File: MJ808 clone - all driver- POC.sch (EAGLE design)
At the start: 38 parts, among them IC1 ATTINY4313-MMH, IC2 PRQV8.00CR1510Y00L, IC6 MCP2515, IC7 MAX16820, IC8 MCP2561-2, IC9 TPS709-Q1, K1 CRTL, Q1 PMV213SN,215, X1 22-23-2021, X2 22-23-2021

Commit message: - updated values for LED1 and LED2, re-generated gerbers
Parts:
- LED1: value XMLBWT-00-0000-0000U20E2 -> LTST-C281KRKT
- LED2: value XMLBWT-00-0000-0000U20E2 -> LTST-C281KGKT
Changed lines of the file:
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@@
 <part name="IC9" library="TPS709-q1 5V LDO" deviceset="TPS709-Q1" device="" value="TPS709-Q1"/>
 <part name="R1" library="rcl" library_urn="urn:adsk.eagle:library:334" deviceset="R-EU_" device="R0402" package3d_urn="urn:adsk.eagle:package:23547/1" value="10k"/>
-<part name="LED1" library="led" library_urn="urn:adsk.eagle:library:259" deviceset="LED" device="CHIP-LED0805" package3d_urn="urn:adsk.eagle:package:15818/1" value="XMLBWT-00-0000-0000U20E2 "/>
-<part name="LED2" library="led" library_urn="urn:adsk.eagle:library:259" deviceset="LED" device="CHIP-LED0805" package3d_urn="urn:adsk.eagle:package:15818/1" value="XMLBWT-00-0000-0000U20E2 "/>
+<part name="LED1" library="led" library_urn="urn:adsk.eagle:library:259" deviceset="LED" device="CHIP-LED0805" package3d_urn="urn:adsk.eagle:package:15818/1" value="LTST-C281KRKT"/>
+<part name="LED2" library="led" library_urn="urn:adsk.eagle:library:259" deviceset="LED" device="CHIP-LED0805" package3d_urn="urn:adsk.eagle:package:15818/1" value="LTST-C281KGKT"/>
 <part name="R3" library="rcl" library_urn="urn:adsk.eagle:library:334" deviceset="R-EU_" device="R0402" package3d_urn="urn:adsk.eagle:package:23547/1" value="10k"/>
 <part name="R4" library="rcl" library_urn="urn:adsk.eagle:library:334" deviceset="R-EU_" device="R0402" package3d_urn="urn:adsk.eagle:package:23547/1" value="10k"/>

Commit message: - sized down ground plane of ICs to make soldering easier - corrected tname and bname positions
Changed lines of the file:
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@@
 <?xml version="1.0" encoding="utf-8"?>
 <!DOCTYPE eagle SYSTEM "eagle.dtd">
-<eagle version="8.5.0">
+<eagle version="8.6.1">
 <drawing>
 <settings>

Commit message: - added pulldown on 5V LDO enable pin
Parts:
- added R5: 10k, rcl:R-EU_R0402
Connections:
- net EN: now also R5.2
- net GND: now also R5.1
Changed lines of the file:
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@@
 <part name="C5" library="rcl" library_urn="urn:adsk.eagle:library:334" deviceset="C-EU" device="C0402" package3d_urn="urn:adsk.eagle:package:23626/1" value="0.1μF"/>
 <part name="C1" library="rcl" library_urn="urn:adsk.eagle:library:334" deviceset="C-EU" device="C0402" package3d_urn="urn:adsk.eagle:package:23626/1" value="0.1μF"/>
-<part name="R11" library="rcl" library_urn="urn:adsk.eagle:library:334" deviceset="R-EU_" device="R0402" package3d_urn="urn:adsk.eagle:package:23547/1" value="10k"/>
-<part name="R7" library="rcl" library_urn="urn:adsk.eagle:library:334" deviceset="R-EU_" device="R0402" package3d_urn="urn:adsk.eagle:package:23547/1" value="10k"/>
-<part name="R2" library="rcl" library_urn="urn:adsk.eagle:library:334" deviceset="R-EU_" device="R0402" package3d_urn="urn:adsk.eagle:package:23547/1" value="10k"/>
+<part name="R11" library="rcl" library_urn="urn:adsk.eagle:library:334" deviceset="R-EU_" device="R0402" package3d_urn="urn:adsk.eagle:package:23547/2" value="10k"/>
+<part name="R7" library="rcl" library_urn="urn:adsk.eagle:library:334" deviceset="R-EU_" device="R0402" package3d_urn="urn:adsk.eagle:package:23547/2" value="10k"/>
+<part name="R2" library="rcl" library_urn="urn:adsk.eagle:library:334" deviceset="R-EU_" device="R0402" package3d_urn="urn:adsk.eagle:package:23547/2" value="10k"/>
 <part name="LSP1" library="solpad" library_urn="urn:adsk.eagle:library:364" deviceset="LSP10" device="" package3d_urn="urn:adsk.eagle:package:26501/1"/>
 <part name="LSP2" library="solpad" library_urn="urn:adsk.eagle:library:364" deviceset="LSP10" device="" package3d_urn="urn:adsk.eagle:package:26501/1"/>
@@
 <part name="IC2" library="PRQV8.00CR1510Y00L - 8MHz resonator" deviceset="PRQV" device="" value=" PRQV8.00CR1510Y00L"/>
 <part name="PROG" library="SPI 1.27mm 10pin header" deviceset="SPI-1.27-10-PIN-HEADER" device=""/>
-<part name="R9" library="rcl" library_urn="urn:adsk.eagle:library:334" deviceset="R-EU_" device="R0402" package3d_urn="urn:adsk.eagle:package:23547/1" value="330"/>
-<part name="R8" library="rcl" library_urn="urn:adsk.eagle:library:334" deviceset="R-EU_" device="R0402" package3d_urn="urn:adsk.eagle:package:23547/1" value="330"/>
-<part name="R6" library="rcl" library_urn="urn:adsk.eagle:library:334" deviceset="R-EU_" device="R0402" package3d_urn="urn:adsk.eagle:package:23547/1" value="330"/>
-<part name="R12" library="rcl" library_urn="urn:adsk.eagle:library:334" deviceset="R-EU_" device="R0402" package3d_urn="urn:adsk.eagle:package:23547/1" value="10k"/>
+<part name="R9" library="rcl" library_urn="urn:adsk.eagle:library:334" deviceset="R-EU_" device="R0402" package3d_urn="urn:adsk.eagle:package:23547/2" value="330"/>
+<part name="R8" library="rcl" library_urn="urn:adsk.eagle:library:334" deviceset="R-EU_" device="R0402" package3d_urn="urn:adsk.eagle:package:23547/2" value="330"/>
+<part name="R6" library="rcl" library_urn="urn:adsk.eagle:library:334" deviceset="R-EU_" device="R0402" package3d_urn="urn:adsk.eagle:package:23547/2" value="330"/>
+<part name="R12" library="rcl" library_urn="urn:adsk.eagle:library:334" deviceset="R-EU_" device="R0402" package3d_urn="urn:adsk.eagle:package:23547/2" value="10k"/>
 <part name="MOSI" library="signal testpoint" deviceset="TP" device="" value="cs"/>
 <part name="MISO" library="signal testpoint" deviceset="TP" device="" value="cs"/>
 <part name="IC9" library="TPS709-q1 5V LDO" deviceset="TPS709-Q1" device="" value="TPS709-Q1"/>
-<part name="R1" library="rcl" library_urn="urn:adsk.eagle:library:334" deviceset="R-EU_" device="R0402" package3d_urn="urn:adsk.eagle:package:23547/1" value="10k"/>
-<part name="LED1" library="led" library_urn="urn:adsk.eagle:library:259" deviceset="LED" device="CHIP-LED0805" package3d_urn="urn:adsk.eagle:package:15818/1" value="LTST-C281KRKT"/>
-<part name="LED2" library="led" library_urn="urn:adsk.eagle:library:259" deviceset="LED" device="CHIP-LED0805" package3d_urn="urn:adsk.eagle:package:15818/1" value="LTST-C281KGKT"/>
-<part name="R3" library="rcl" library_urn="urn:adsk.eagle:library:334" deviceset="R-EU_" device="R0402" package3d_urn="urn:adsk.eagle:package:23547/1" value="10k"/>
-<part name="R4" library="rcl" library_urn="urn:adsk.eagle:library:334" deviceset="R-EU_" device="R0402" package3d_urn="urn:adsk.eagle:package:23547/1" value="10k"/>
+<part name="R1" library="rcl" library_urn="urn:adsk.eagle:library:334" deviceset="R-EU_" device="R0402" package3d_urn="urn:adsk.eagle:package:23547/2" value="10k"/>
+<part name="LED1" library="led" library_urn="urn:adsk.eagle:library:259" deviceset="LED" device="CHIP-LED0805" package3d_urn="urn:adsk.eagle:package:15818/2" value="LTST-C281KRKT"/>
+<part name="LED2" library="led" library_urn="urn:adsk.eagle:library:259" deviceset="LED" device="CHIP-LED0805" package3d_urn="urn:adsk.eagle:package:15818/2" value="LTST-C281KGKT"/>
+<part name="R3" library="rcl" library_urn="urn:adsk.eagle:library:334" deviceset="R-EU_" device="R0402" package3d_urn="urn:adsk.eagle:package:23547/2" value="10k"/>
+<part name="R4" library="rcl" library_urn="urn:adsk.eagle:library:334" deviceset="R-EU_" device="R0402" package3d_urn="urn:adsk.eagle:package:23547/2" value="10k"/>
 <part name="K1" library="Seeed-Switch" library_urn="urn:adsk.eagle:library:476" deviceset="SMD-SWITCH-TACTILE-SPST-NO(4P-D6.0MM)" device="" package3d_urn="urn:adsk.eagle:package:32987/1" value="CRTL"/>
+<part name="R5" library="rcl" library_urn="urn:adsk.eagle:library:334" deviceset="R-EU_" device="R0402" package3d_urn="urn:adsk.eagle:package:23547/2" value="10k"/>
 </parts>
 <sheets>
@@
 <instance part="R4" gate="G$1" x="228.6" y="226.06" rot="R180"/>
 <instance part="K1" gate="G$1" x="111.76" y="200.66"/>
+<instance part="R5" gate="G$1" x="264.16" y="307.34" rot="R90"/>
 </instances>
 <busses>
@@
 <segment>
 <pinref part="IC9" gate="G$1" pin="IN"/>
-<wire x1="256.54" y1="314.96" x2="259.08" y2="314.96" width="0.1524" layer="91"/>
-<label x="259.08" y="314.96" size="1.778" layer="95"/>
+<wire x1="256.54" y1="314.96" x2="269.24" y2="314.96" width="0.1524" layer="91"/>
+<label x="269.24" y="314.96" size="1.778" layer="95"/>
 </segment>
 </net>
@@
 <wire x1="124.46" y1="213.36" x2="124.46" y2="218.44" width="0.1524" layer="91"/>
 <label x="124.46" y="218.44" size="1.778" layer="95"/>
+</segment>
+<segment>
+<pinref part="R5" gate="G$1" pin="1"/>
+<wire x1="264.16" y1="302.26" x2="264.16" y2="297.18" width="0.1524" layer="91"/>
+<label x="264.16" y="297.18" size="1.778" layer="95"/>
 </segment>
 </net>
@@
 <segment>
 <pinref part="IC9" gate="G$1" pin="EN"/>
-<wire x1="256.54" y1="312.42" x2="259.08" y2="312.42" width="0.1524" layer="91"/>
-<label x="259.08" y="312.42" size="1.778" layer="95"/>
+<wire x1="256.54" y1="312.42" x2="264.16" y2="312.42" width="0.1524" layer="91"/>
+<label x="269.24" y="312.42" size="1.778" layer="95"/>
+<pinref part="R5" gate="G$1" pin="2"/>
+<wire x1="264.16" y1="312.42" x2="269.24" y2="312.42" width="0.1524" layer="91"/>
+<junction x="264.16" y="312.42"/>
 </segment>
 <segment>
@@
 packages will not be understood (or retained) with this version.
 </note>
+<note version="8.4" severity="warning">
+Since Version 8.4, EAGLE supports properties for SPICE simulation.
+Probes in schematics and SPICE mapping objects found in parts and library devices
+will not be understood with this version. Update EAGLE to the latest version
+for full support of SPICE simulation.
+</note>
 </compatibility>

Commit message: - replaced LED connector with 2.54mm pitch header
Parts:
- removed LSP1, LSP2: LSP10, solpad:LSP10
- added X3: 22-23-2021, con-molex:22-23-2021
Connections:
- removed net N$3: L1.2, LSP2.MP
- new net LED+: L1.2, X3-1.S
- net CSN: now also X3-2.S; no longer LSP1.MP
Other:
- moved on the sheet: C1, C5, C6, C7, C8, CS, D1, IC1, IC2, IC6, IC7, IC8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

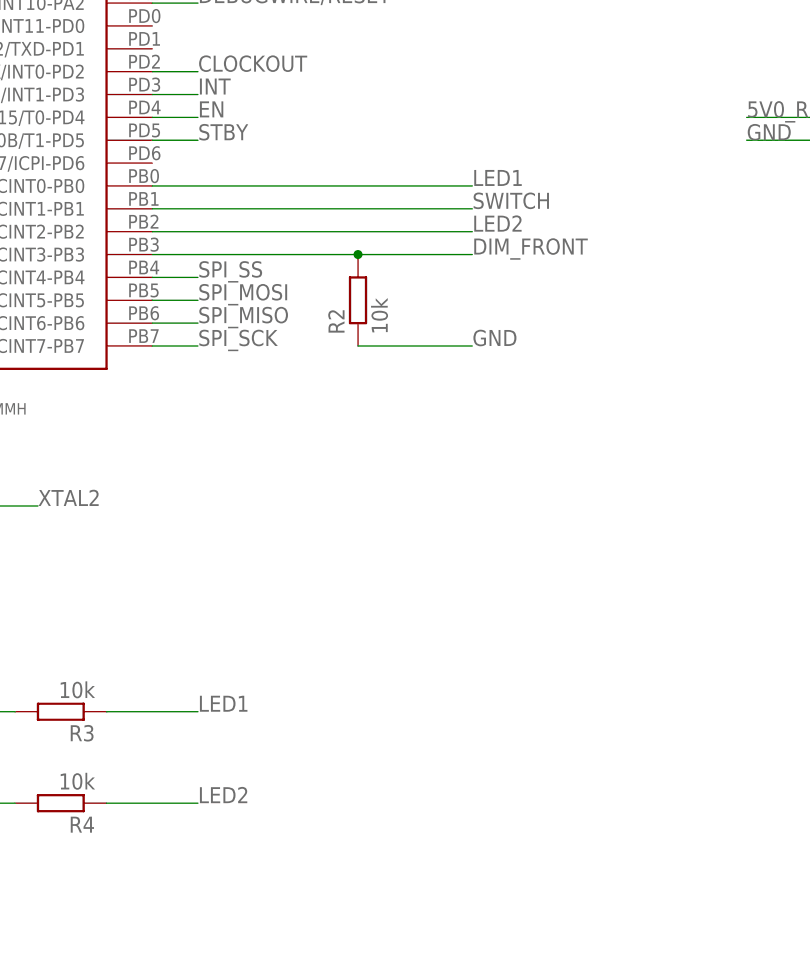
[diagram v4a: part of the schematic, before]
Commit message: - corrected LED plus and minus signs on connector
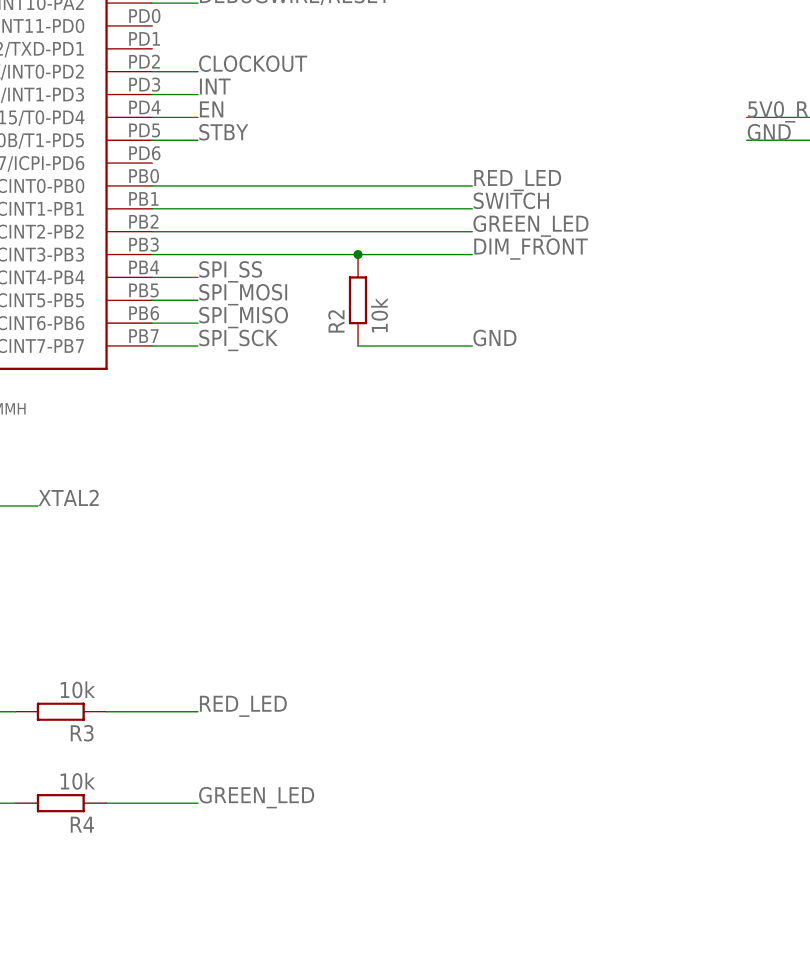
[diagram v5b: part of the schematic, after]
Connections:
- net LED1 renamed RED_LED
- net LED2 renamed GREEN_LED
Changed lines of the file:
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@@
 </segment>
 </net>
-<net name="LED1" class="0">
+<net name="RED_LED" class="0">
 <segment>
 <pinref part="R3" gate="G$1" pin="1"/>
@@
 </segment>
 </net>
-<net name="LED2" class="0">
+<net name="GREEN_LED" class="0">
 <segment>
 <pinref part="R4" gate="G$1" pin="1"/>

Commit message: - added passives xls calculator, added XLampXML2 datasheet, VLS6045EX-150M Inductor inductor - replaced LDO - updated BOM - recreated gerbers
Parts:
- removed CS, MISO, MOSI: cs, signal testpoint:TP
- removed IC8: MCP2561-2, MCP2561-2 - High-Speed CAN Transceiver:MCP2561-2
- removed IC9: TPS709-Q1, TPS709-q1 5V LDO:TPS709-Q1
- removed PROG: SPI-1.27-10-PIN-HEADER, SPI 1.27mm 10pin header:SPI-1.27-10-PIN-HEADER
- removed SCK: sck, signal testpoint:TP
- added C2, C3: 1μF, rcl:C-EUC0402
- added C4: 0.1μF, rcl:C-EUC0402
- added CONN1: SPI-1.27-10-PIN-HEADER, SPI 1.27mm 10pin header:SPI-1.27-10-PIN-HEADER
- added IC3, IC5: LP38693SD-5.0/NOPB, LP38693 5V LDO:LP38693
- added IC4: MCP2515, MCP2515-I-ML - Standalonce CAN Controller with SPI Interface:MCP2515-I-ML
- added TP1: sck, signal testpoint:TP
- added TP2, TP3, TP4: cs, signal testpoint:TP
- C5: value 0.1μF -> 1μF
- C6: value 47μF / 15V+ -> 1μF; device rcl:C-EUC0805 -> rcl:C-EUC0402
- C7: value 1μF -> 0.1μF
- C8: value 0.1μF -> 47μF / 15V+; device rcl:C-EUC0402 -> rcl:C-EUC0805
- IC6: value MCP2515 -> MCP2561-2; device MCP2515-I-ML - Standalonce CAN Controller with SPI Interface:MCP2515-I-ML -> MCP2561-2 - High-Speed CAN Transceiver:MCP2561-2
- L1: value AISC-1210HS-330K-T2 -> VLS6045EX-150M-CA; device eagle-ltspice:LL3225M -> SparkFun-Coils:INDUCTOR-SRN6045-33UH
- LED1: value LTST-C281KRKT -> LTST-C170KRKT
- LED2: value LTST-C281KGKT -> LTST-C170KGKT
- R10: value 0.25 / 2W -> 10k; device rcl:R-EU_R1206 -> rcl:R-EU_R0402
- R11: value 10k -> 0.15 / 1W; device rcl:R-EU_R0402 -> rcl:R-EU_R1210
- R5: value 10k -> 330
- R9: value 330 -> 10k
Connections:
- net 5V0: now also C2.1, CONN1.VCC, IC3.OUT; no longer C7.1, IC7.VCC, PROG.VCC
- net 5V0_REG: now also C4.1, C7.1, IC4.VDD, IC5.OUT, IC6.VCC; no longer C8.1, IC6.VDD, IC8.VCC, IC9.OUT
- net CANH: now also IC6.CANH; no longer IC8.CANH
- net CANL: now also IC6.CANL; no longer IC8.CANL
- net CLOCKOUT: now also IC4.OSC1; no longer IC6.OSC1
- net CSN: now also R11.1; no longer R10.1
- net DEBUGWIRE/RESET: now also CONN1.RESET; no longer PROG.RESET
- net DIM_FRONT: now also R4.2; no longer R2.2
- net DIM_FRONT_GATE: now also R10.1; no longer R11.1
- net EN: now also IC5.EN, R9.2; no longer IC9.EN, R5.2
- net GATE: now also R10.2; no longer R11.2
- net GND: now also C2.2, C3.1, C4.2, CONN1.GND, IC3.GND, IC4.GND, IC5.GND, R4.1, R9.1; no longer IC8.GND, IC9.GND, PROG.GND, R2.1, R5.1
- net GREEN_LED: now also R3.1; no longer R4.1
- net INT: now also IC4.!INT!; no longer IC6.!INT!
- net N$4: now also R2.2; no longer R3.2
- net N$5: now also R3.2; no longer R4.2
- net RED_LED: now also R2.1; no longer R3.1
- net RXCAN: now also IC4.RXCAN, IC6.RXD; no longer IC6.RXCAN, IC8.RXD
- net SCK: now also CONN1.SPI_SCK, IC4.SCK, R5.1; no longer IC6.SCK, PROG.SPI_SCK, R6.1
- net SI: now also CONN1.SPI_MOSI, IC4.SI, R6.1; no longer IC6.SI, PROG.SPI_MOSI, R8.1
- net SO: now also CONN1.SPI_MISO, IC4.SO, R8.1; no longer IC6.SO, PROG.SPI_MISO, R9.1
- net SPI_MISO: now also R8.2, TP4.TP$1; no longer MISO.TP$1, R9.2
- net SPI_MOSI: now also R6.2, TP3.TP$1; no longer MOSI.TP$1, R8.2
- net SPI_SCK: now also R5.2, TP1.TP$1; no longer R6.2, SCK.TP$1
- net SPI_SS: now also IC4.!CS!, TP2.TP$1; no longer CS.TP$1, IC6.!CS!
- net STBY: now also IC6.STBY; no longer IC8.STBY
- net TXCAN: now also IC4.TXCAN, IC6.TXD; no longer IC6.TXCAN, IC8.TXD
- net VBAT: now also C3.2, C8.1, IC3.EN, IC3.IN, IC5.IN, R11.2; no longer IC9.IN, R10.2
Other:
- note added: "CAN infrastructure"
- note added: "power supply for CAN infrastructure"
- note added: "power supply for microcontroller"
- note added: "white LED driver"
- moved on the sheet: C1, C5, C6, C7, C8, D1, IC1, IC2, IC7, K1, LED1, LED2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
